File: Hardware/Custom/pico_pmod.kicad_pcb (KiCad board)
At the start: 2 copper layers, 50 x 37 mm, 44 parts, among them J1 Conn_02x06_Odd_Even, J2 Conn_02x06_Odd_Even, J3 Conn_02x06_Odd_Even, J4 USB_C_Receptacle_USB2.0, J5 Conn_01x04, SW1 SW_Push, SW2 SW_Push, U1 RP2040, U2 W25Q128JVS, U3 NCP1117-3.3_SOT223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

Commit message: Add logo on front of board and straight PMod tracks
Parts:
- added G***: LOGO, jjh:j2h_small, F.Cu at (157.0, 81.2)
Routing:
- net GPIO_5: track 32.3 -> 31.4 mm
- net GPIO_4: track 35.5 -> 34.5 mm
- net GPIO_7: track 32.8 -> 31.8 mm
- net GPIO_6: track 35.8 -> 34.9 mm
- net GPIO_3: track 31.9 -> 31.3 mm

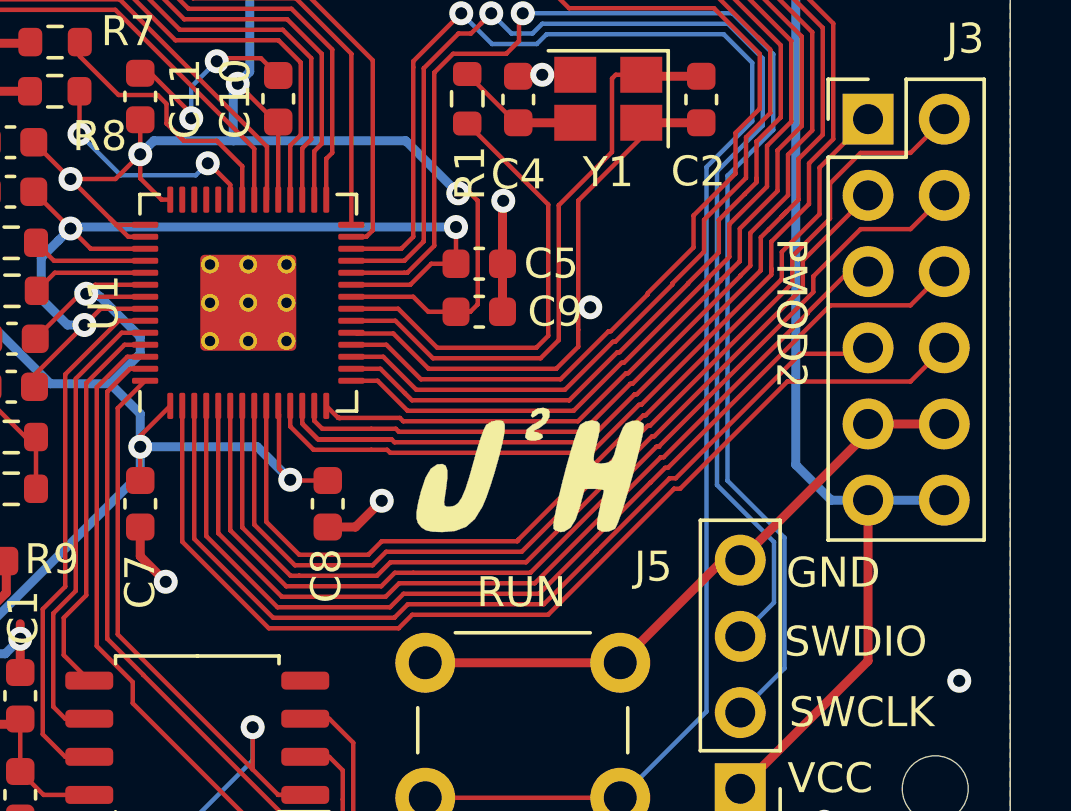
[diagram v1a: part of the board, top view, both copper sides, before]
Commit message: edit the PMOD traces to straighten them
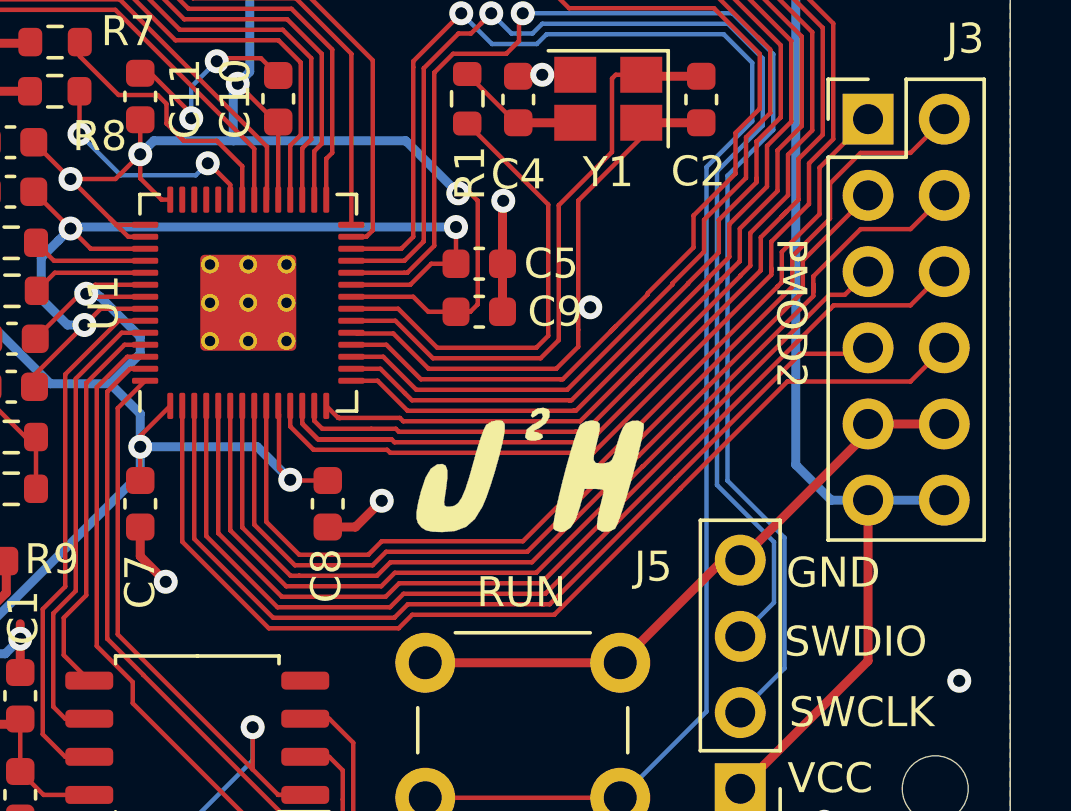
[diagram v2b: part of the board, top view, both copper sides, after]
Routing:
- net GPIO_10: track 38.1 -> 38.8 mm
- net GPIO_3: track 31.3 -> 31.9 mm
